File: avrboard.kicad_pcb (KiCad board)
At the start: 2 copper layers, 20 parts, among them IC1 ATMEGA328P-P, P1 FTDI, P2 ICSP, SW1 RESET, U1 7805, X1 16MHz

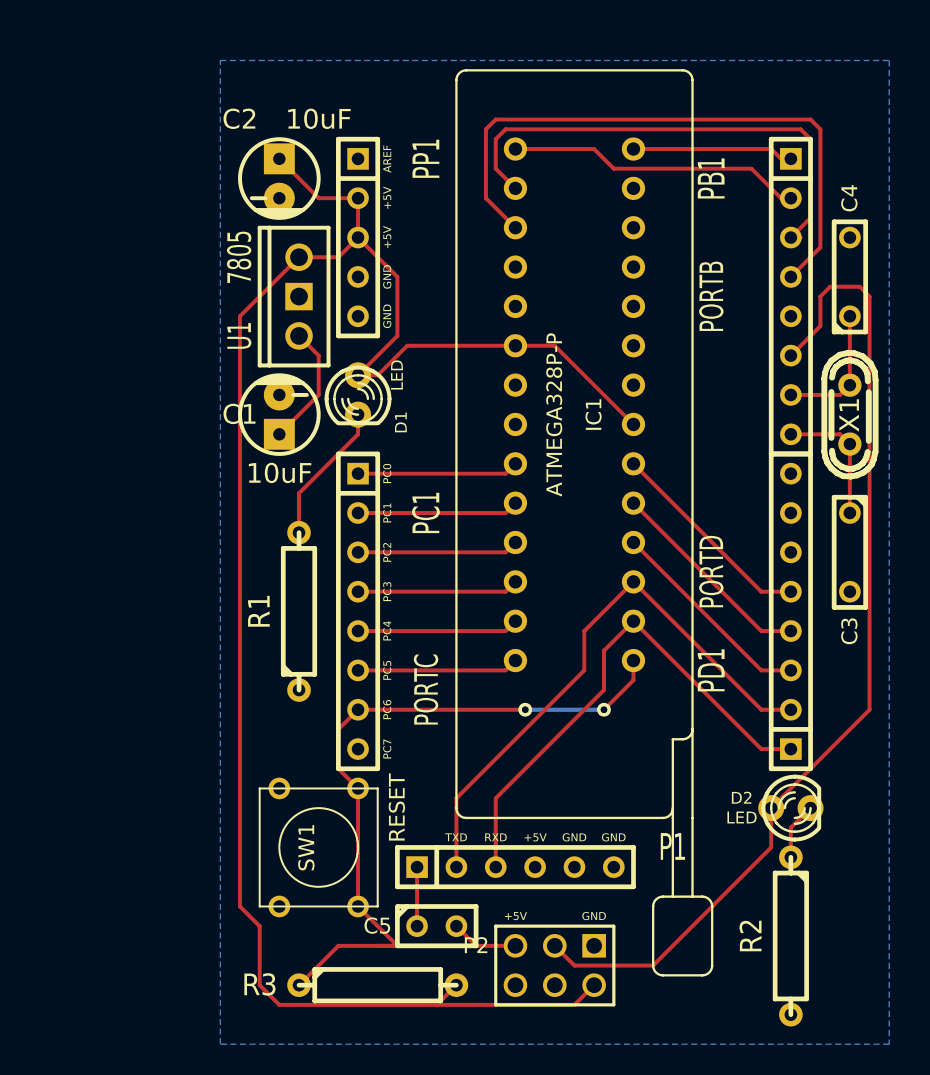
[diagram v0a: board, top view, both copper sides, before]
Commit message: Finish routing the PCB traces.
Got a little ugly towards the end to get the traces to the programming
headers, but not too bad. Might revise later.
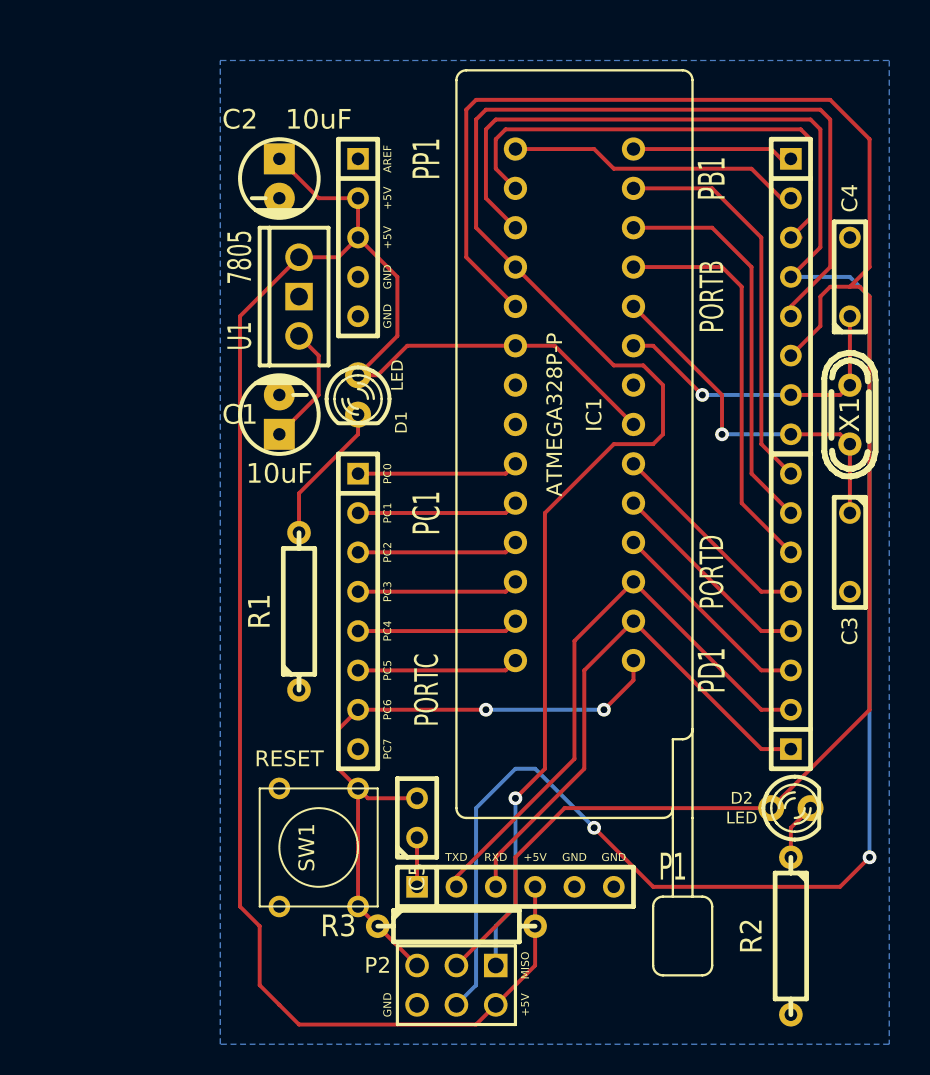
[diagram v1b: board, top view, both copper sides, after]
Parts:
- moved C5 7.10 mm to (137.2, 84.5), turned to 90 degrees
- moved P2 6.48 mm to (139.7, 95.2)
- moved R3 6.35 mm to (139.7, 91.4)
- moved P1 1.27 mm to (143.5, 88.9)
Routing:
- net /PB4: track 0.00 -> 103.8 mm, vias 0 -> 1
- net /PB3: track 39.6 -> 125.0 mm, vias 0 -> 2
- net /PB5: track 64.1 -> 121.8 mm
- net /PD5: track 0.00 -> 26.0 mm
- net /PD7: track 0.00 -> 25.6 mm
- net /PD6: track 0.00 -> 25.6 mm
- net /PB7: track 8.52 -> 23.6 mm, vias 0 -> 1
- net /RESET: track 55.3 -> 43.1 mm
- net /PB6: track 8.52 -> 20.0 mm, vias 0 -> 1
- net /RXD: track 33.1 -> 34.4 mm
- net /TXD: track 36.7 -> 38.0 mm
- net /+5V: track 118.2 -> 119.3 mm
- net Net-(C5-Pad1): track 3.81 -> 3.18 mm
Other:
- board text added: "MISO"

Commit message: Connect AREF to +5V.
No sensible way to route AREF, so for now the compromise is to just route
it to +5V so the ADC can be *usable* when configured to use an external
voltage source (e.g. for testing after programming) while not being
particularly accurate (since this is going to be noisy.)

Given that the primary purpose of this board is programming and then
post-programming brief testing, with the chip ultimately ending up in
a dedicated PCB design, this seems like a reasonable compromise.
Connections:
- IC1 pad 21: Net-(IC1-Pad21) -> /+5V
- PP1 pad 1: /AREF -> /+5V
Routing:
- net /+5V: track 119.3 -> 124.3 mm
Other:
- board text removed: "AREF"

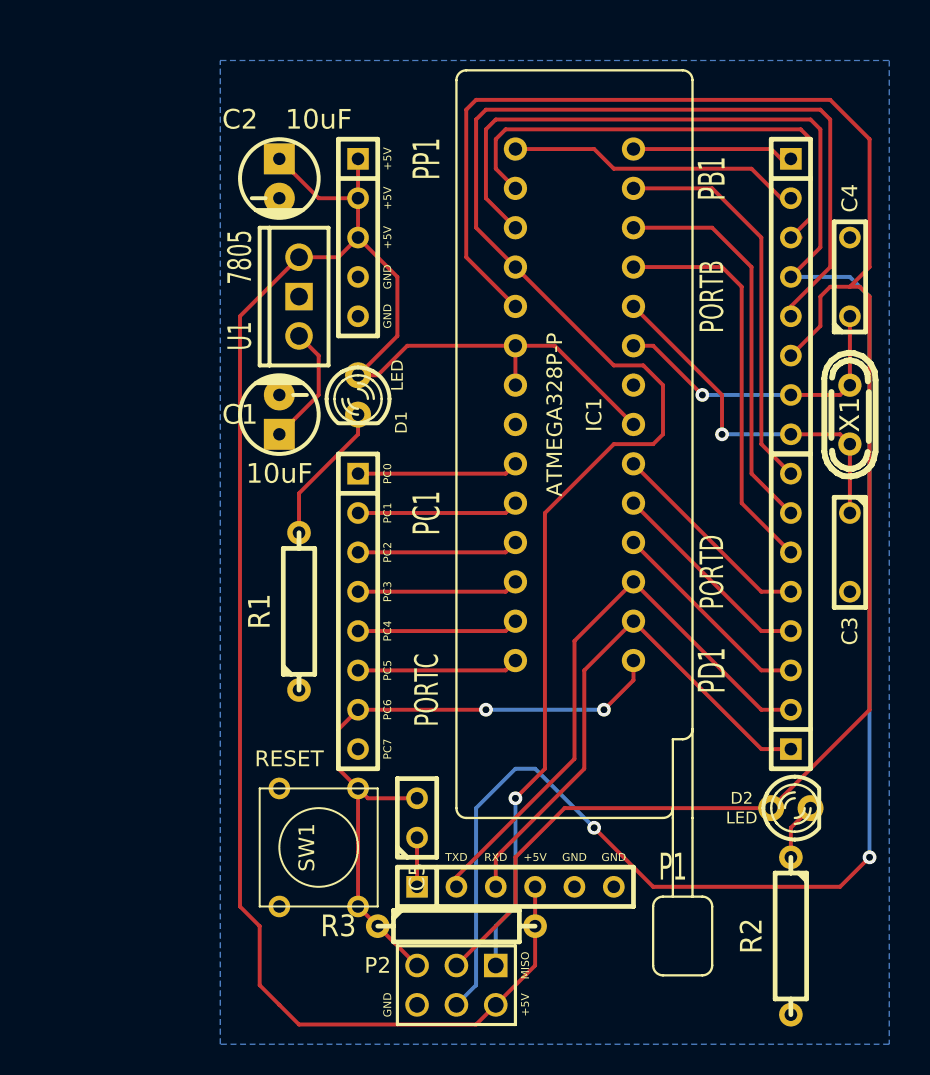
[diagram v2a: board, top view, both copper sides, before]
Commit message: Remove the power regulator from the design.
Since this board is primarily for programming, it's fine to just get
power from the ICSP or FTDI headers in most cases, which should already
be regulated to 5V.

There was nowhere in the design for the power barrel jack to go anyway,
so this saves a little more space and also allows the ICSP header to move
closer to the SPI pins and thus fix some of the more awkward routes
from the previous iteration.
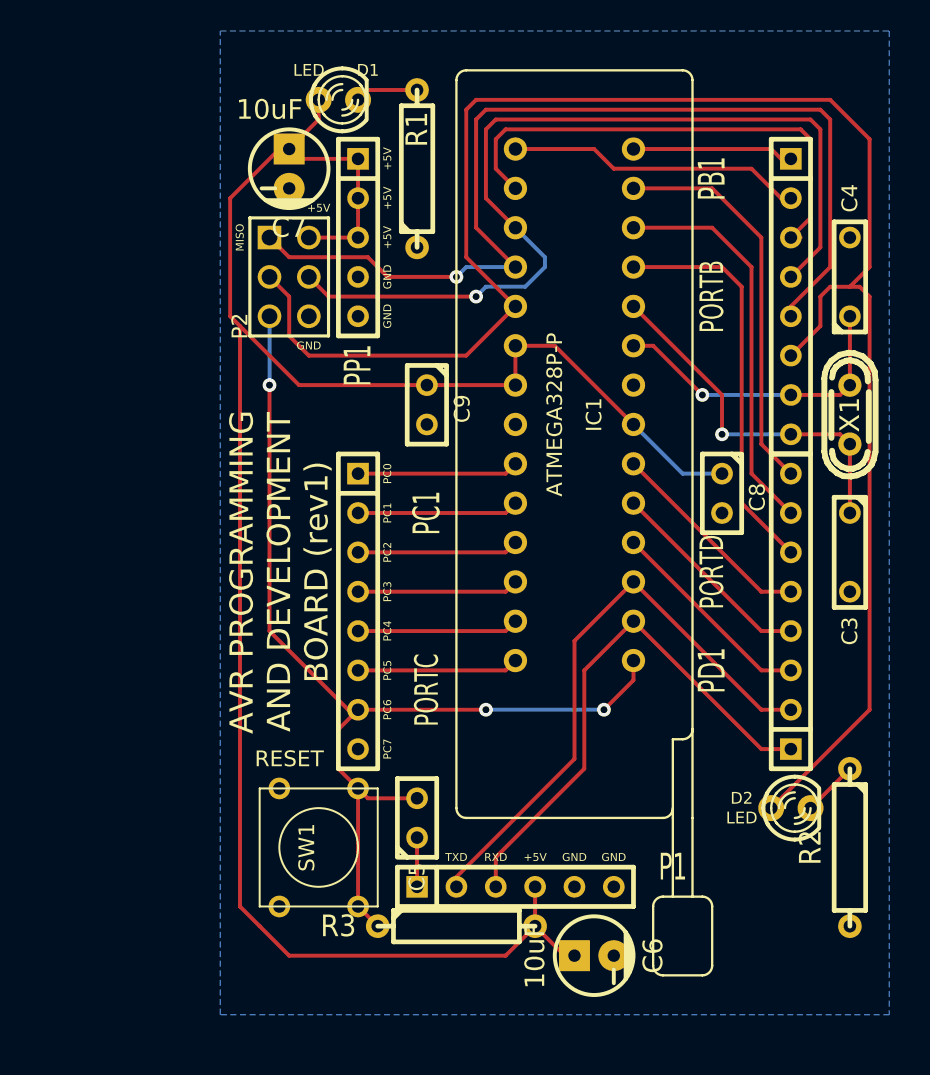
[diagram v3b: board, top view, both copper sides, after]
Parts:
- removed C1, C2: 10uF, capacitors:CP_5x6mm
- removed U1: 7805, discret:LM78XXV
- added C6: 10uF, Capacitors:CP_5x11mm, F.Cu at (148.6, 93.3)
- added C7: 10uF, Capacitors:CP_5x11mm, F.Cu at (128.9, 42.5)
- added C8: 100nF, Discret:C1, F.Cu at (156.8, 63.5)
- added C9: 100nF, Discret:C1, F.Cu at (137.8, 57.8)
- moved P2 47.0 mm to (128.9, 49.5), turned to 270 degrees
- moved R1 29.6 mm to (137.2, 42.5)
- moved D1 19.1 mm to (132.1, 38.1), turned to 0 degrees
- moved R2 6.87 mm to (165.1, 86.4)
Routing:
- net /PB3: track 125.0 -> 59.5 mm, vias 2 -> 1
- net /PB4: track 103.8 -> 64.9 mm
- net /RESET: track 43.1 -> 67.6 mm, vias 2 -> 3
- net /+5V: track 124.3 -> 133.7 mm
- net VCC: track 7.93 -> 0.00 mm
- net /PB5: track 121.8 -> 116.1 mm
- net Net-(D1-Pad2): track 9.20 -> 4.07 mm
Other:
- board text added: "AVR PROGRAMMING AND DEVELOPMENT BOARD (rev1)"

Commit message: More port labels and some track routing adjustments.
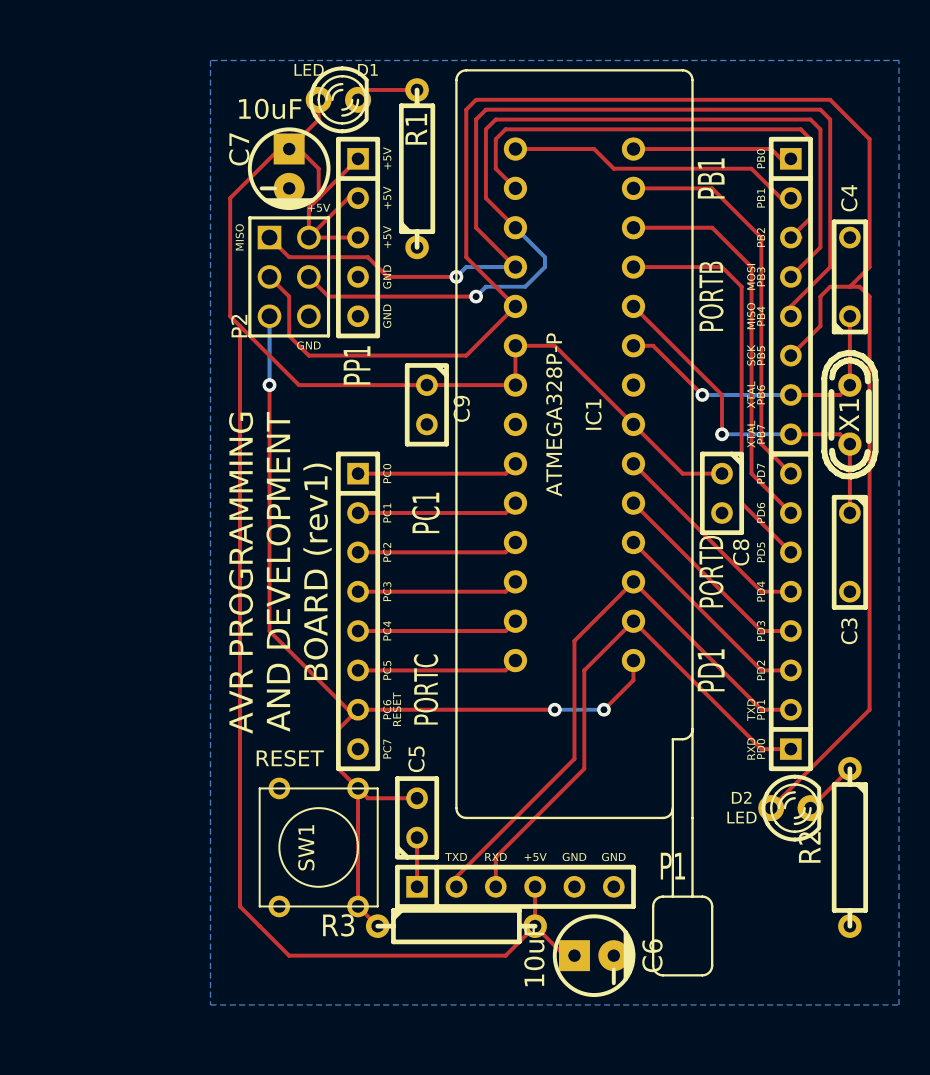
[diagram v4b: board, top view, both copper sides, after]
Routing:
- net /+5V: track 133.7 -> 139.5 mm
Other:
- board text added: "MOSI"
- board text added: "PB0"
- board text added: "PB1"
- board text added: "PB2"
- board text added: "PB3"
- board text added: "PB4"
- board text added: "PB5"
- board text added: "PB6"
- board text added: "PB7"
- board text added: "PD0"
- board text added: "PD1"
- board text added: "PD2"
- board text added: "PD3"
- board text added: "PD4"
- board text added: "PD5"
- board text added: "PD6"
- board text added: "PD7"
- board text added: "RESET"
- board text added: "SCK"
- board text added: "XTAL"
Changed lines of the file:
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@@
     (links 70)
     (no_connects 0)
-    (area 123.632686 35.27425 169.243829 99.060001)
+    (area 123.632686 35.27425 169.243829 96.520001)
     (thickness 1.6)
-    (drawings 22)
-    (tracks 171)
+    (drawings 46)
+    (tracks 176)
     (zones 0)
     (modules 21)
@@
     (descr "Condensateur e = 1 pas")
     (tags C)
-    (fp_text reference C5 (at -3.81 0 90) (layer F.SilkS)
+    (fp_text reference C5 (at 3.81 0 90) (layer F.SilkS)
       (effects (font (size 1.016 1.016) (thickness 0.2032)))
     )
@@
     (at 128.905 42.545 180)
     (descr "Capacitor, pol, cyl 5x11mm")
-    (fp_text reference C7 (at 0 -3.81 180) (layer F.SilkS)
+    (fp_text reference C7 (at 3.175 1.27 270) (layer F.SilkS)
       (effects (font (thickness 0.3048)))
     )
@@
     (descr "Condensateur e = 1 pas")
     (tags C)
-    (fp_text reference C8 (at 0.254 -2.286 270) (layer F.SilkS)
-      (effects (font (size 1.016 1.016) (thickness 0.2032)))
-    )
-    (fp_text value 100nF (at 0 -2.286 270) (layer F.SilkS) hide
+    (fp_text reference C8 (at 3.81 -1.27 270) (layer F.SilkS)
+      (effects (font (size 1.016 1.016) (thickness 0.2032)))
+    )
+    (fp_text value 100nF (at 7.62 -1.27 270) (layer F.SilkS) hide
       (effects (font (size 1.016 1.016) (thickness 0.2032)))
     )
@@
     )
   )
+  (gr_text RESET (at 135.89 77.47 90) (layer F.SilkS)
+    (effects (font (size 0.5094 0.5094) (thickness 0.1137)))
+  )
+  (gr_text SCK (at 158.75 54.61 90) (layer F.SilkS)
+    (effects (font (size 0.5094 0.5094) (thickness 0.1137)))
+  )
+  (gr_text MOSI (at 158.75 49.53 90) (layer F.SilkS)
+    (effects (font (size 0.5094 0.5094) (thickness 0.1137)))
+  )
+  (gr_text MISO (at 158.75 52.07 90) (layer F.SilkS)
+    (effects (font (size 0.5094 0.5094) (thickness 0.1137)))
+  )
+  (gr_text XTAL (at 158.75 57.15 90) (layer F.SilkS)
+    (effects (font (size 0.5094 0.5094) (thickness 0.1137)))
+  )
+  (gr_text XTAL (at 158.75 59.69 90) (layer F.SilkS)
+    (effects (font (size 0.5094 0.5094) (thickness 0.1137)))
+  )
+  (gr_text TXD (at 158.75 77.47 90) (layer F.SilkS)
+    (effects (font (size 0.5094 0.5094) (thickness 0.1137)))
+  )
+  (gr_text RXD (at 158.75 80.01 90) (layer F.SilkS)
+    (effects (font (size 0.5094 0.5094) (thickness 0.1137)))
+  )
+  (gr_text PD0 (at 159.385 80.01 90) (layer F.SilkS)
+    (effects (font (size 0.5094 0.5094) (thickness 0.1137)))
+  )
+  (gr_text PD1 (at 159.385 77.47 90) (layer F.SilkS)
+    (effects (font (size 0.5094 0.5094) (thickness 0.1137)))
+  )
+  (gr_text PD2 (at 159.385 74.93 90) (layer F.SilkS)
+    (effects (font (size 0.5094 0.5094) (thickness 0.1137)))
+  )
+  (gr_text PD3 (at 159.385 72.39 90) (layer F.SilkS)
+    (effects (font (size 0.5094 0.5094) (thickness 0.1137)))
+  )
+  (gr_text PD4 (at 159.385 69.85 90) (layer F.SilkS)
+    (effects (font (size 0.5094 0.5094) (thickness 0.1137)))
+  )
+  (gr_text PD5 (at 159.385 67.31 90) (layer F.SilkS)
+    (effects (font (size 0.5094 0.5094) (thickness 0.1137)))
+  )
+  (gr_text PD6 (at 159.385 64.77 90) (layer F.SilkS)
+    (effects (font (size 0.5094 0.5094) (thickness 0.1137)))
+  )
+  (gr_text PD7 (at 159.385 62.23 90) (layer F.SilkS)
+    (effects (font (size 0.5094 0.5094) (thickness 0.1137)))
+  )
+  (gr_text PB7 (at 159.385 59.69 90) (layer F.SilkS)
+    (effects (font (size 0.5094 0.5094) (thickness 0.1137)))
+  )
+  (gr_text PB6 (at 159.385 57.15 90) (layer F.SilkS)
+    (effects (font (size 0.5094 0.5094) (thickness 0.1137)))
+  )
+  (gr_text PB5 (at 159.385 54.61 90) (layer F.SilkS)
+    (effects (font (size 0.5094 0.5094) (thickness 0.1137)))
+  )
+  (gr_text PB4 (at 159.385 52.07 90) (layer F.SilkS)
+    (effects (font (size 0.5094 0.5094) (thickness 0.1137)))
+  )
+  (gr_text PB3 (at 159.385 49.53 90) (layer F.SilkS)
+    (effects (font (size 0.5094 0.5094) (thickness 0.1137)))
+  )
+  (gr_text PB2 (at 159.385 46.99 90) (layer F.SilkS)
+    (effects (font (size 0.5094 0.5094) (thickness 0.1137)))
+  )
+  (gr_text PB1 (at 159.385 44.45 90) (layer F.SilkS)
+    (effects (font (size 0.5094 0.5094) (thickness 0.1137)))
+  )
+  (gr_text PB0 (at 159.385 41.91 90) (layer F.SilkS)
+    (effects (font (size 0.5094 0.5094) (thickness 0.1137)))
+  )
   (gr_text "AVR PROGRAMMING\nAND DEVELOPMENT\nBOARD (rev1)" (at 128.27 68.58 90) (layer F.SilkS)
     (effects (font (size 1.5 1.5) (thickness 0.3)))
@@
     (effects (font (size 0.5094 0.5094) (thickness 0.1137)))
   )
+  (segment (start 128.905 41.275) (end 129.54 41.275) (width 0.254) (layer F.Cu) (net 1) (status C00000))
+  (segment (start 129.54 41.275) (end 130.81 42.545) (width 0.254) (layer F.Cu) (net 1) (status 400000))
+  (segment (start 130.81 42.545) (end 130.81 44.45) (width 0.254) (layer F.Cu) (net 1))
+  (segment (start 130.175 46.99) (end 130.175 45.085) (width 0.254) (layer F.Cu) (net 1) (status 400000))
+  (segment (start 130.175 45.085) (end 130.81 44.45) (width 0.254) (layer F.Cu) (net 1))
+  (segment (start 130.81 44.45) (end 133.35 41.91) (width 0.254) (layer F.Cu) (net 1) (status 800000))
+  (segment (start 130.175 46.99) (end 130.81 46.99) (width 0.254) (layer F.Cu) (net 1) (status C00000))
+  (segment (start 130.175 46.99) (end 132.715 44.45) (width 0.254) (layer F.Cu) (net 1) (status C00000))
+  (segment (start 132.715 44.45) (end 133.35 44.45) (width 0.254) (layer F.Cu) (net 1) (status C00000))
+  (segment (start 151.13 59.055) (end 154.305 62.23) (width 0.254) (layer F.Cu) (net 1))
+  (segment (start 154.305 62.23) (end 156.845 62.23) (width 0.254) (layer F.Cu) (net 1))
   (segment (start 127 91.44) (end 128.905 93.345) (width 0.254) (layer F.Cu) (net 1))
   (segment (start 125.73 90.17) (end 127 91.44) (width 0.254) (layer F.Cu) (net 1))
@@
   (segment (start 130.81 38.1) (end 130.81 39.37) (width 0.254) (layer F.Cu) (net 1))
   (segment (start 130.81 39.37) (end 128.905 41.275) (width 0.254) (layer F.Cu) (net 1))
-  (segment (start 133.35 41.91) (end 129.54 41.91) (width 0.254) (layer F.Cu) (net 1))
-  (segment (start 129.54 41.91) (end 128.905 41.275) (width 0.254) (layer F.Cu) (net 1))
   (segment (start 130.175 46.99) (end 133.35 46.99) (width 0.254) (layer F.Cu) (net 1))
-  (segment (start 156.845 62.23) (end 154.305 62.23) (width 0.254) (layer B.Cu) (net 1))
-  (segment (start 154.305 62.23) (end 151.13 59.055) (width 0.254) (layer B.Cu) (net 1))
   (segment (start 137.795 56.515) (end 143.51 56.515) (width 0.254) (layer F.Cu) (net 1))
-  (segment (start 133.35 46.99) (end 133.35 44.45) (width 0.254) (layer F.Cu) (net 1))
   (segment (start 146.05 53.975) (end 151.13 59.055) (width 0.254) (layer F.Cu) (net 1))
   (segment (start 143.51 53.975) (end 146.05 53.975) (width 0.254) (layer F.Cu) (net 1))
   (segment (start 144.78 91.44) (end 144.78 88.9) (width 0.254) (layer F.Cu) (net 1))
-  (segment (start 133.35 44.45) (end 133.35 41.91) (width 0.254) (layer F.Cu) (net 1))
   (segment (start 143.51 56.515) (end 143.51 53.975) (width 0.254) (layer F.Cu) (net 1))
   (segment (start 160.02 41.275) (end 151.13 41.275) (width 0.254) (layer F.Cu) (net 2))
@@
   (segment (start 132.08 78.74) (end 133.35 77.47) (width 0.254) (layer F.Cu) (net 23))
   (segment (start 133.35 82.55) (end 132.08 81.28) (width 0.254) (layer F.Cu) (net 23))
-  (via (at 141.605 77.47) (size 0.889) (layers F.Cu B.Cu) (net 23))
-  (segment (start 141.605 77.47) (end 149.225 77.47) (width 0.254) (layer B.Cu) (net 23))
+  (via (at 146.05 77.47) (size 0.889) (layers F.Cu B.Cu) (net 23))
+  (segment (start 146.05 77.47) (end 149.225 77.47) (width 0.254) (layer B.Cu) (net 23))
   (via (at 149.225 77.47) (size 0.889) (layers F.Cu B.Cu) (net 23))
   (segment (start 149.225 77.47) (end 151.13 75.565) (width 0.254) (layer F.Cu) (net 23))
   (segment (start 151.13 75.565) (end 151.13 74.295) (width 0.254) (layer F.Cu) (net 23))
-  (segment (start 133.35 77.47) (end 141.605 77.47) (width 0.254) (layer F.Cu) (net 23))
+  (segment (start 133.35 77.47) (end 146.05 77.47) (width 0.254) (layer F.Cu) (net 23))
   (segment (start 133.985 83.185) (end 133.35 82.55) (width 0.254) (layer F.Cu) (net 23))
   (segment (start 137.16 83.185) (end 133.985 83.185) (width 0.254) (layer F.Cu) (net 23))
@@
   (segment (start 137.16 37.465) (end 133.985 37.465) (width 0.254) (layer F.Cu) (net 28))
   (segment (start 133.985 37.465) (end 133.35 38.1) (width 0.254) (layer F.Cu) (net 28))
-  (segment (start 162.56 83.82) (end 165.1 81.28) (width 0.254) (layer F.Cu) (net 29) (status C00000))
+  (segment (start 162.56 83.82) (end 165.1 81.28) (width 0.254) (layer F.Cu) (net 29))
   (zone (net 26) (net_name GND) (layer B.Cu) (hatch edge 0.508)
     (connect_pads (clearance 0.508))
@@
     (polygon
       (pts
-        (xy 124.46 33.655) (xy 167.64 33.655) (xy 167.64 97.155) (xy 124.46 97.155)
+        (xy 123.825 35.56) (xy 123.825 96.52) (xy 168.275 96.52) (xy 168.275 35.56)
       )
     )
